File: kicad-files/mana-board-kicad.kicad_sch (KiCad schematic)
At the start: 39 parts, among them U1 Pico

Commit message: Organize libraries, start rev1
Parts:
- D1: value SK6812MINI -> SK6812MINI-E; footprint Footprints:SK6812-MINI-E-reversed -> Keebio-Parts:SK6812-MINI-E; symbol LED:SK6812MINI -> ManaBoard:SK6812MINI-E
- D10, D11, D12, D2, D3, D4, D5, D6, D7, D8, D9: footprint Footprints:SK6812-MINI-E-reversed -> Keebio-Parts:SK6812-MINI-E; symbol LED:SK6812MINI -> ManaBoard:SK6812MINI-E
- R4, R5: value R_Small -> 5.1k
- TP2: value TestPoint -> PI DM
- TP3: value TestPoint -> PI DP
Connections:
- net GND: now also D1.3 (VSS), D10.3 (VSS), D11.3 (VSS), D12.3 (VSS), D2.3 (VSS), D3.3 (VSS), D4.3 (VSS), D5.3 (VSS), D6.3 (VSS), D7.3 (VSS), D8.3 (VSS), D9.3 (VSS); no longer D1.2 (VSS), D10.2 (VSS), D11.2 (VSS), D12.2 (VSS), D2.2 (VSS), D3.2 (VSS), D4.2 (VSS), D5.2 (VSS), D6.2 (VSS), D7.2 (VSS), D8.2 (VSS), D9.2 (VSS), U1.28 (GND)
- net 5V: now reaches D4.1 (VDD)
- net 5V: now also D1.1 (VDD), D10.1 (VDD), D11.1 (VDD), D12.1 (VDD), D2.1 (VDD), D3.1 (VDD), D5.1 (VDD), D6.1 (VDD), D7.1 (VDD), D8.1 (VDD), D9.1 (VDD), U1.40 (VBUS), USB1.A4 (VBUS), USB1.A9 (VBUS), USB1.B4 (VBUS), USB1.B9 (VBUS); no longer D5.3 (DIN)
- net RGBDATA: now reaches U1.34 (GPIO28_ADC2)
- net RGBDATA: now also D1.4 (DIN); no longer D1.3 (DIN)
- new net: D4.2 (DOUT), D5.4 (DIN)
- new net: D3.2 (DOUT), D4.4 (DIN)
- new net: D2.2 (DOUT), D3.4 (DIN)
- new net: D5.2 (DOUT), D6.4 (DIN)
- new net: D11.2 (DOUT), D12.4 (DIN)
- new net: D10.2 (DOUT), D11.4 (DIN)
- new net: D7.2 (DOUT), D8.4 (DIN)
- new net: D6.2 (DOUT), D7.4 (DIN)
- new net: D10.4 (DIN), D9.2 (DOUT)
- new net: D8.2 (DOUT), D9.4 (DIN)
- new net: D1.2 (DOUT), D2.4 (DIN)
- new net 3.3V: U1.36 (3V3)
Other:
- moved on the sheet: D1, D10, D11, D12, D2, D3, D4, D5, D6, D7, D8, D9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

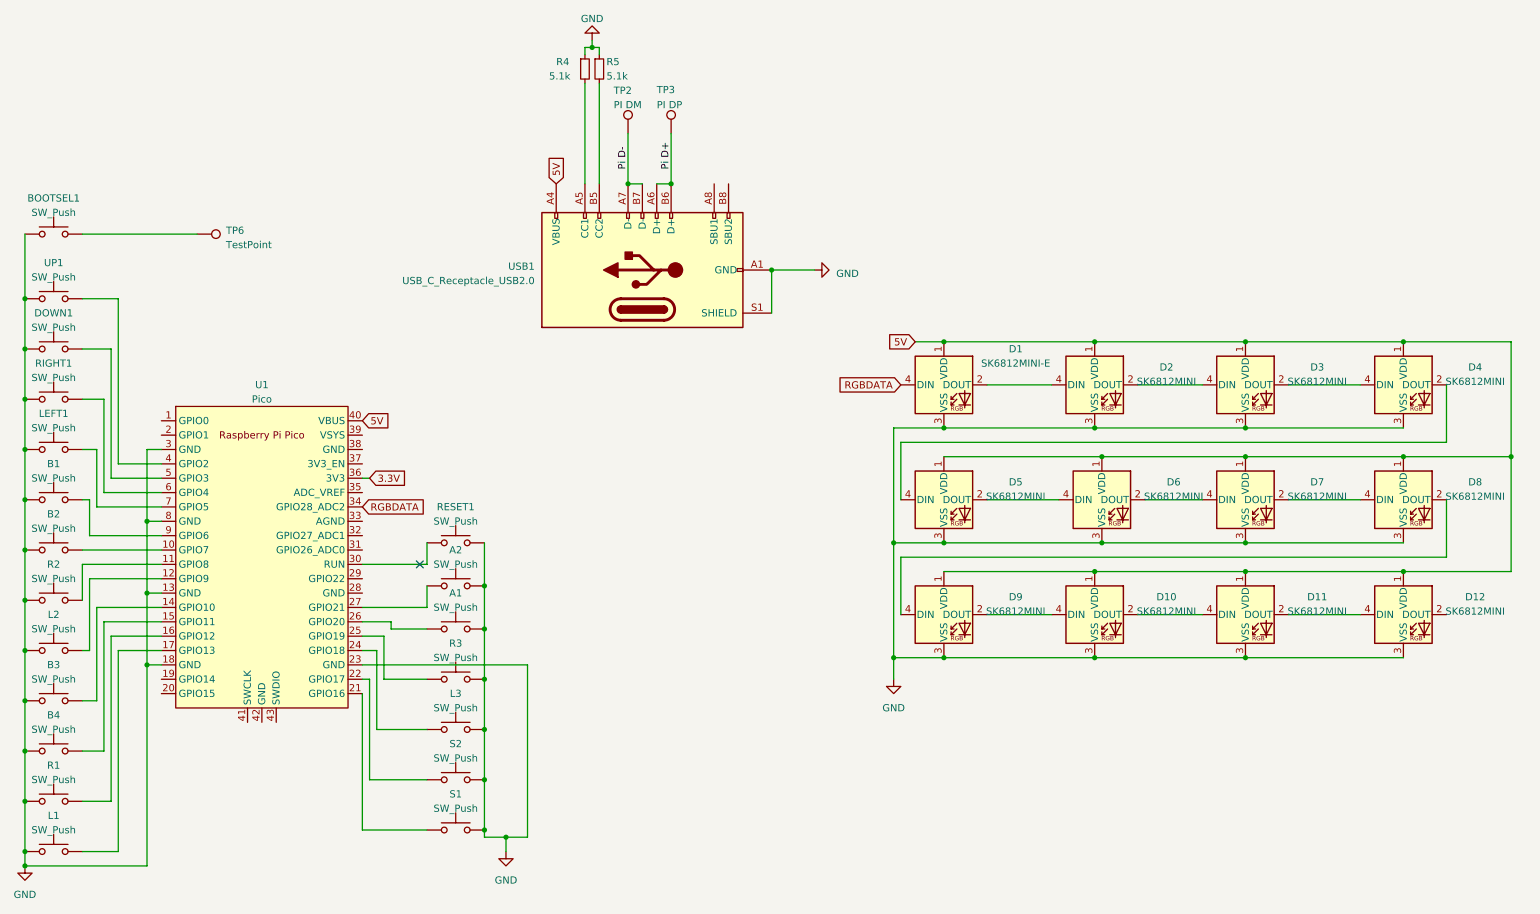
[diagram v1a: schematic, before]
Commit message: First pass at wiring rev1
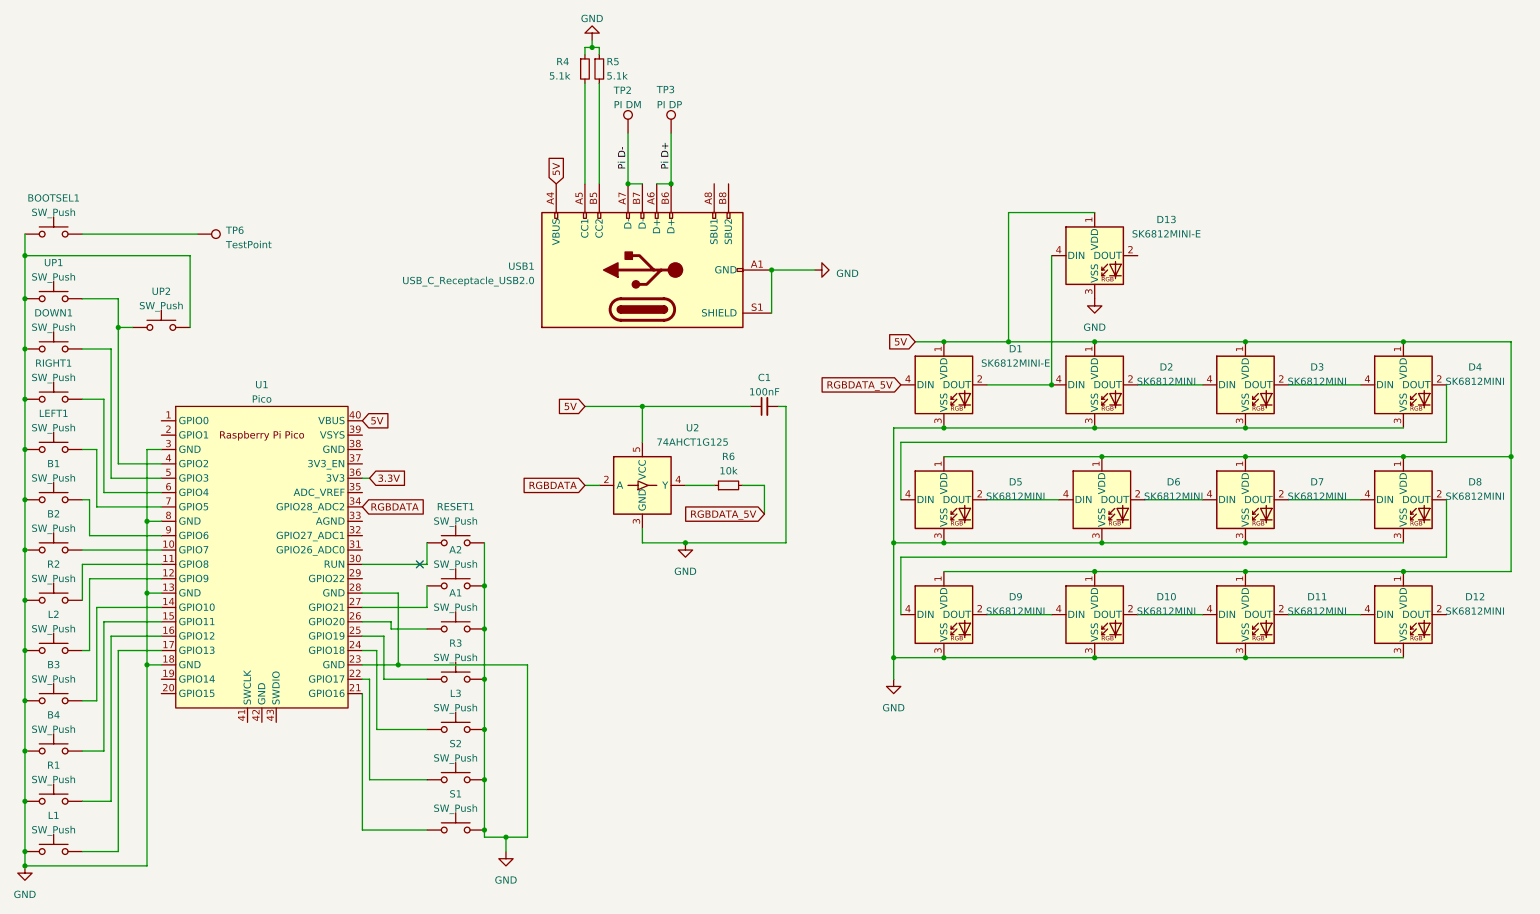
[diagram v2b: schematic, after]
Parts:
- added C1: 100nF, Capacitor_SMD:C_1206_3216Metric_Pad1.33x1.80mm_HandSolder, symbol Device:C_Small
- added D13: SK6812MINI-E, ManaBoard:SK6812-MINI-E, symbol ManaBoard:SK6812MINI-E
- added R6: 10k, Resistor_SMD:R_1206_3216Metric_Pad1.30x1.75mm_HandSolder, symbol Device:R_Small
- added U2: 74AHCT1G125, Package_TO_SOT_SMD:SOT-23-5, symbol Logic_LevelTranslator:SN74LV1T34DBV
- added UP2: SW_Push, ManaBoard:SW_Kailh_Choc_V2, symbol Switch:SW_Push
- B1, B2, B3, B4, DOWN1, L1, L2, LEFT1, R1, R2, RIGHT1, UP1: footprint Switch_Keyboard_Kailh:SW_Kailh_Choc_V2_1.00u -> ManaBoard:SW_Kailh_Choc_V2
- D1, D10, D11, D12, D2, D3, D4, D5, D6, D7, D8, D9: footprint Keebio-Parts:SK6812-MINI-E -> ManaBoard:SK6812-MINI-E
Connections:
- net 5V: now also C1.1, D13.1 (VDD), U2.5 (VCC)
- net GND: now also U1.28 (GND), C1.2, D13.3 (VSS), U2.3 (GND), UP2.2
- net RGBDATA: now also U2.2 (A); no longer D1.4 (DIN)
- net at D1.2 (DOUT), D2.4 (DIN): now also D13.4 (DIN)
- net at U1.4 (GPIO2), UP1.2: now also UP2.1
- new net: R6.1, U2.4 (Y)
- new net RGBDATA_5V: D1.4 (DIN), R6.2

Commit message: update board a little
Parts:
- added C10, C11, C12, C13, C14, C2, C3, C4, C5, C6, C7, C8, C9: 100nF, Capacitor_SMD:C_1206_3216Metric_Pad1.33x1.80mm_HandSolder, symbol Device:C_Small
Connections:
- net 5V: now also C10.1, C11.1, C12.1, C13.1, C14.1, C2.1, C3.1, C4.1, C5.1, C6.1, C7.1, C8.1, C9.1
- net GND: now also C10.2, C11.2, C12.2, C13.2, C14.2, C2.2, C3.2, C4.2, C5.2, C6.2, C7.2, C8.2, C9.2
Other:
- moved on the sheet: D10, D11, D12, D5, D6, D7, D8, D9

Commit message: Cleaned up routing, cleanup todo
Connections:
- net at D4.2 (DOUT): now also D13.4 (DIN), D2.4 (DIN); no longer D5.4 (DIN)
- net at D3.4 (DIN): now also D1.2 (DOUT); no longer D2.2 (DOUT)
- net at D13.2 (DOUT): now also D5.4 (DIN)
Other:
- moved on the sheet: C14, C3, C4, C5, D13, D2, D3, D4

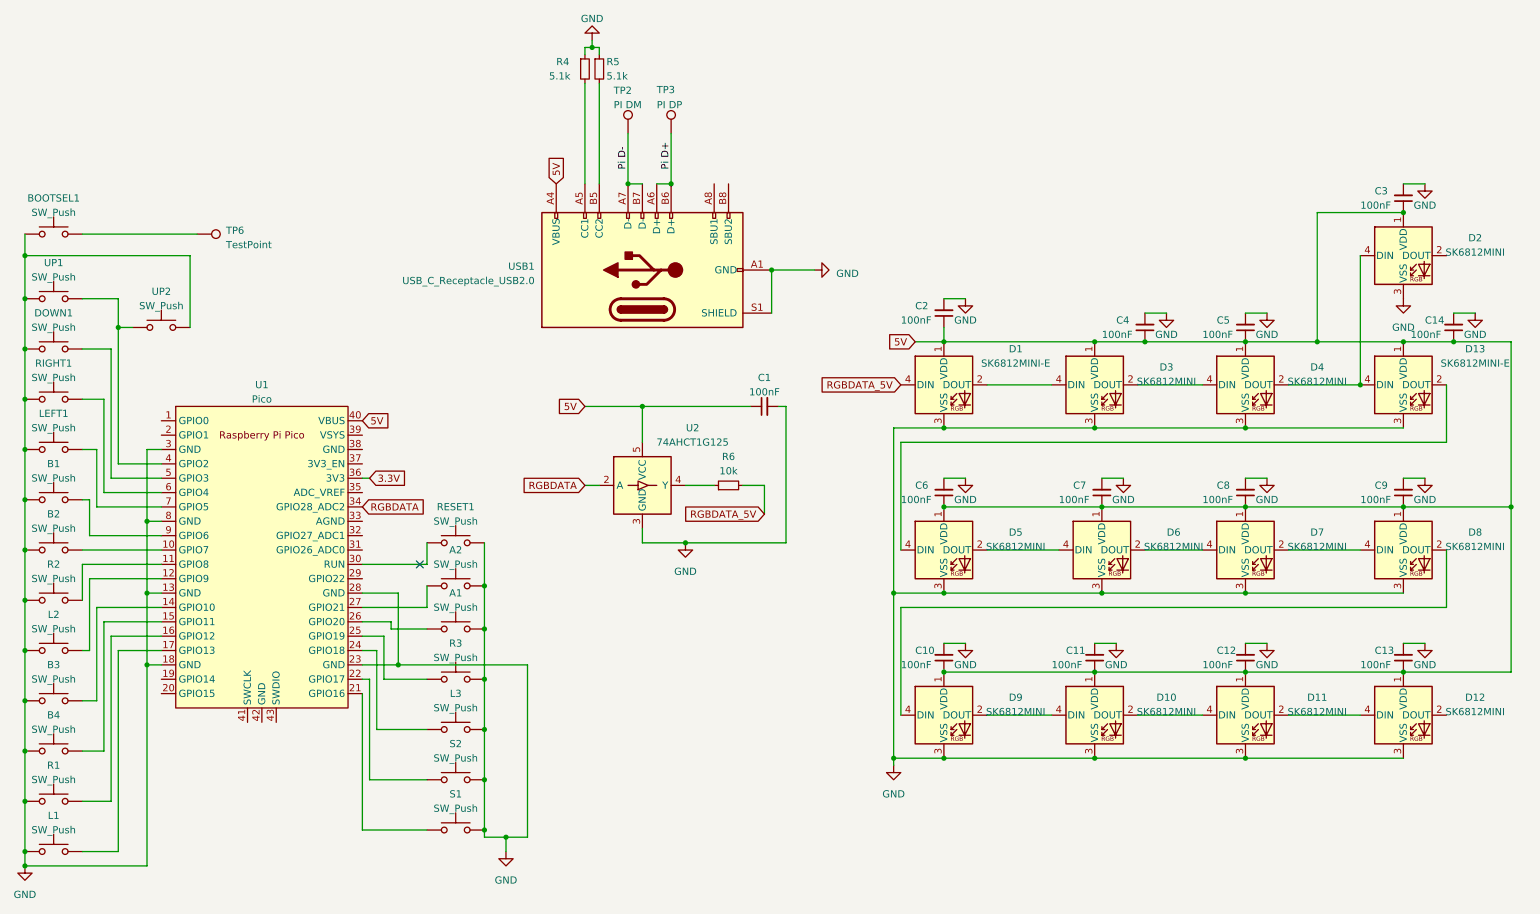
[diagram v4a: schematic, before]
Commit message: Move parallel UP LEDs to the end of the LED chain
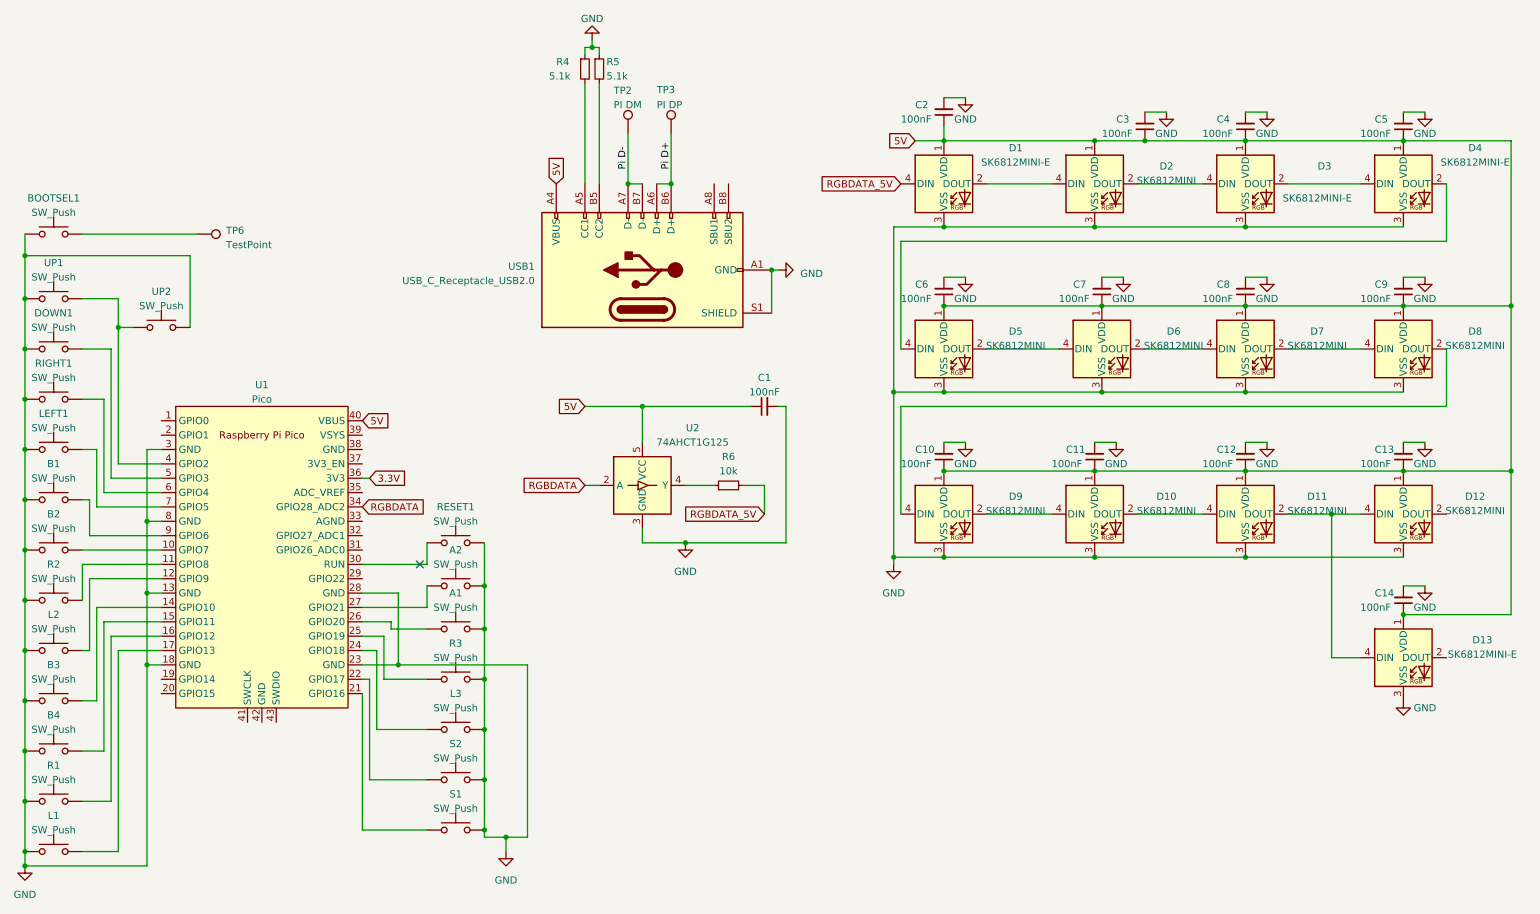
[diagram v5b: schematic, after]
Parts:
- D13: renamed from D2; value SK6812MINI -> SK6812MINI-E
- D3: renamed from D4; value SK6812MINI -> SK6812MINI-E
- renumbered C3 to C14, C4 to C3, C5 to C4, C14 to C5, D3 to D2, D13 to D4
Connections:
- net at D3.2 (DOUT), D4.4 (DIN): no longer D13.4 (DIN)
- net at D11.2 (DOUT), D12.4 (DIN): now also D13.4 (DIN)
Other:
- moved on the sheet: C10, C11, C12, C13, C14, C2, C3, C4, C5, C6, C7, C8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

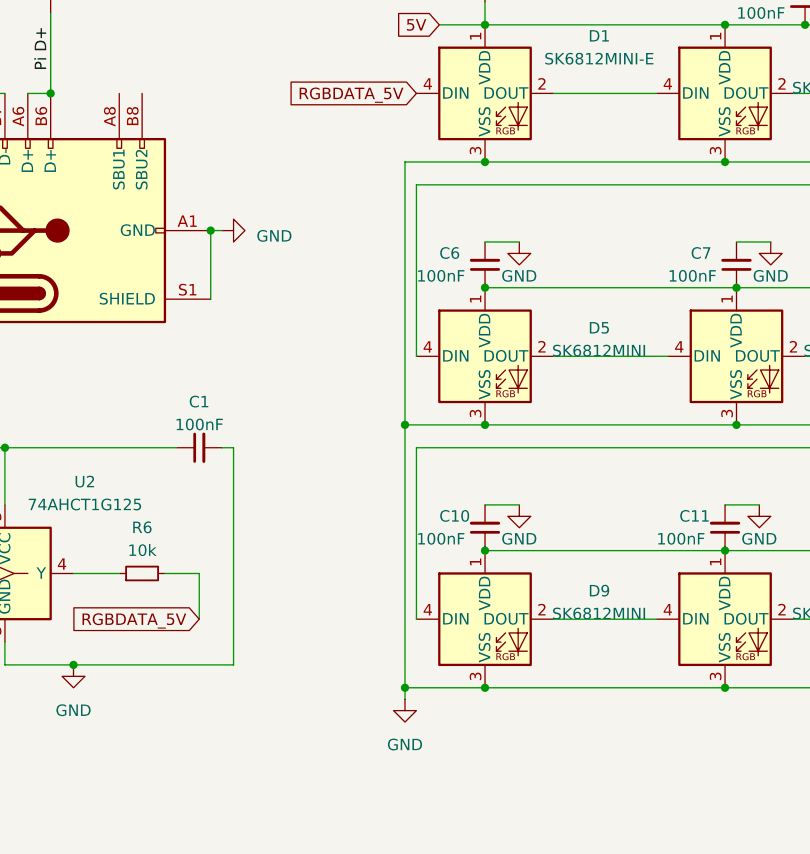
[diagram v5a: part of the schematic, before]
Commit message: reasign capacitor numbers
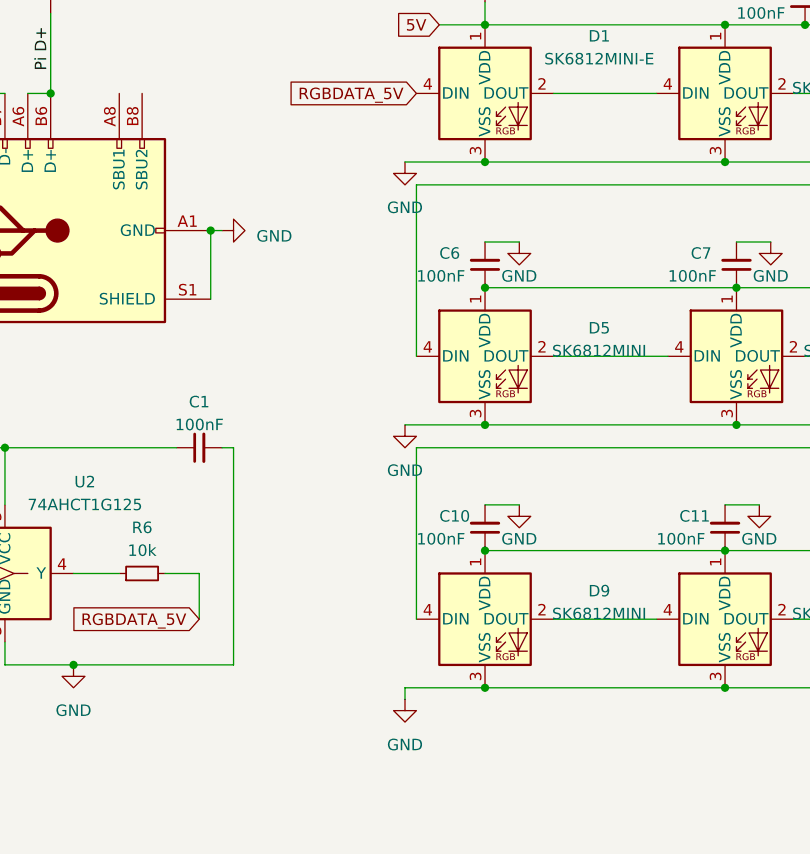
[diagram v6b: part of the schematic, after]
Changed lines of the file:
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@@
   (junction (at 280.67 102.87) (diameter 0) (color 0 0 0 0)
   )
-  (junction (at 171.45 118.11) (diameter 0) (color 0 0 0 0)
-  )
   (junction (at 83.82 137.16) (diameter 0) (color 0 0 0 0)
   )
   (junction (at 180.34 118.11) (diameter 0) (color 0 0 0 0)
-  )
-  (junction (at 171.45 88.9) (diameter 0) (color 0 0 0 0)
   )
   (junction (at 17.78 161.29) (diameter 0) (color 0 0 0 0)
@@
     (stroke (width 0) (type default))
   )
-  (wire (pts (xy 171.45 59.69) (xy 171.45 88.9))
-    (stroke (width 0) (type default))
-  )
   (wire (pts (xy 106.68 137.16) (xy 106.68 167.64))
     (stroke (width 0) (type default))
@@
   )
   (wire (pts (xy 77.47 127) (xy 88.9 127))
-    (stroke (width 0) (type default))
-  )
-  (wire (pts (xy 171.45 88.9) (xy 171.45 118.11))
     (stroke (width 0) (type default))
   )
@@
         (path "/6e72a416-e274-4dce-bf37-eb35fd0240ae"
           (reference "D5") (unit 1)
+        )
+      )
+    )
+  )
+  (symbol (lib_id "power:GND") (at 171.45 88.9 0) (unit 1)
+    (in_bom yes) (on_board yes) (dnp no) (fields_autoplaced)
+    (property "Reference" "#PWR021" (at 171.45 95.25 0)
+      (effects (font (size 1.27 1.27)) hide)
+    )
+    (property "Value" "GND" (at 171.45 93.98 0)
+      (effects (font (size 1.27 1.27)))
+    )
+    (property "Footprint" "" (at 171.45 88.9 0)
+      (effects (font (size 1.27 1.27)) hide)
+    )
+    (property "Datasheet" "" (at 171.45 88.9 0)
+      (effects (font (size 1.27 1.27)) hide)
+    )
+    (pin "1")
+    (instances
+      (project "mana-board-kicad"
+        (path "/6e72a416-e274-4dce-bf37-eb35fd0240ae"
+          (reference "#PWR021") (unit 1)
         )
       )
@@
         )
       )
+    )
+  )
+  (symbol (lib_id "power:GND") (at 171.45 59.69 0) (unit 1)
+    (in_bom yes) (on_board yes) (dnp no) (fields_autoplaced)
+    (property "Reference" "#PWR022" (at 171.45 66.04 0)
+      (effects (font (size 1.27 1.27)) hide)
+    )
+    (property "Value" "GND" (at 171.45 64.77 0)
+      (effects (font (size 1.27 1.27)))
+    )
+    (property "Footprint" "" (at 171.45 59.69 0)
+      (effects (font (size 1.27 1.27)) hide)
+    )
+    (property "Datasheet" "" (at 171.45 59.69 0)
+      (effects (font (size 1.27 1.27)) hide)
+    )
+    (pin "1")
+    (instances
+      (project "mana-board-kicad"
+        (path "/6e72a416-e274-4dce-bf37-eb35fd0240ae"
+          (reference "#PWR022") (unit 1)
+        )
+      )
